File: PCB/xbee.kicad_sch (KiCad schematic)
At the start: 5 parts

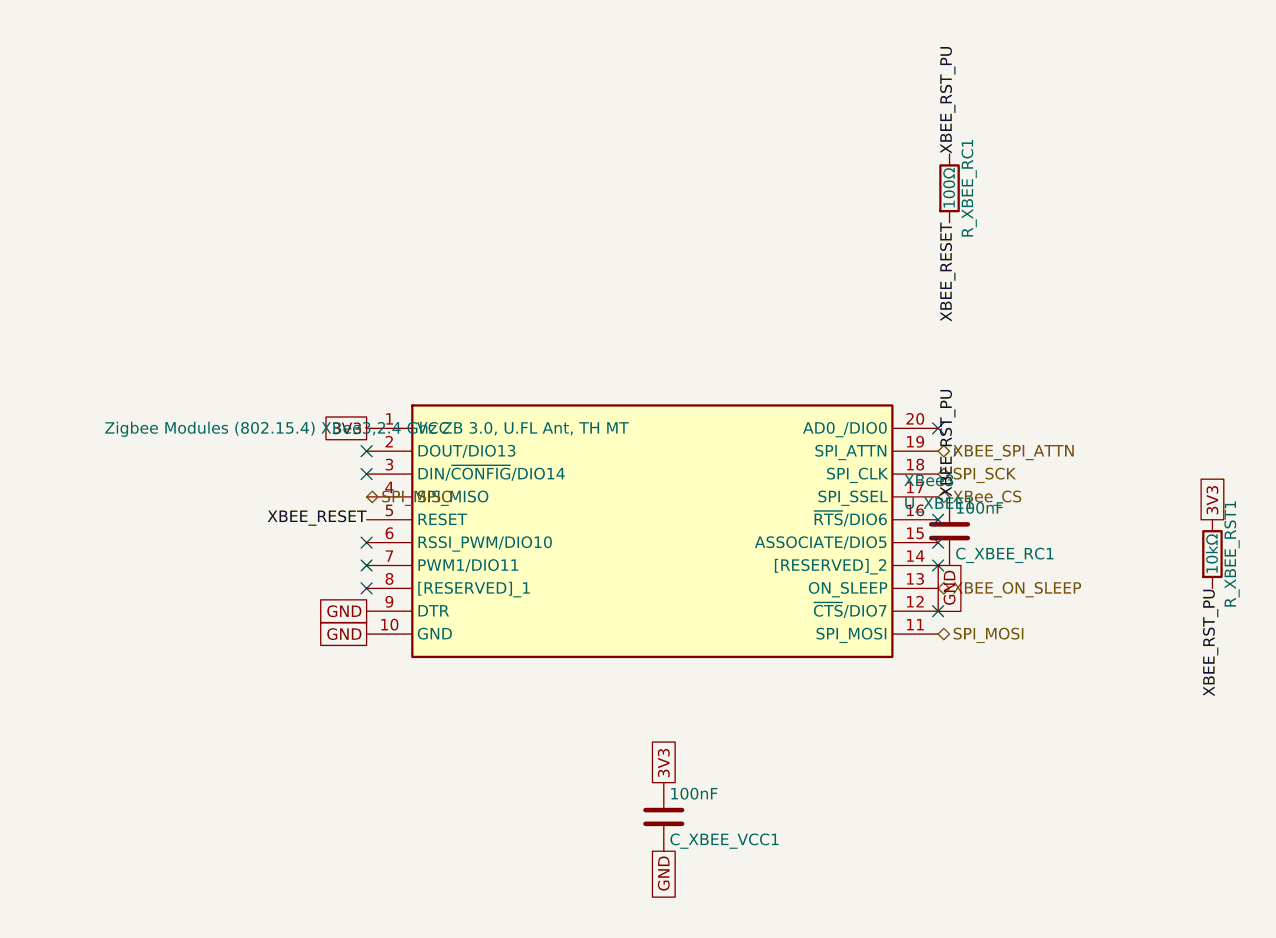
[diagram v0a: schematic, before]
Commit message: refactor: updated gulikit footprint
This updates the gulikit thumbstick footprint to be accurate.
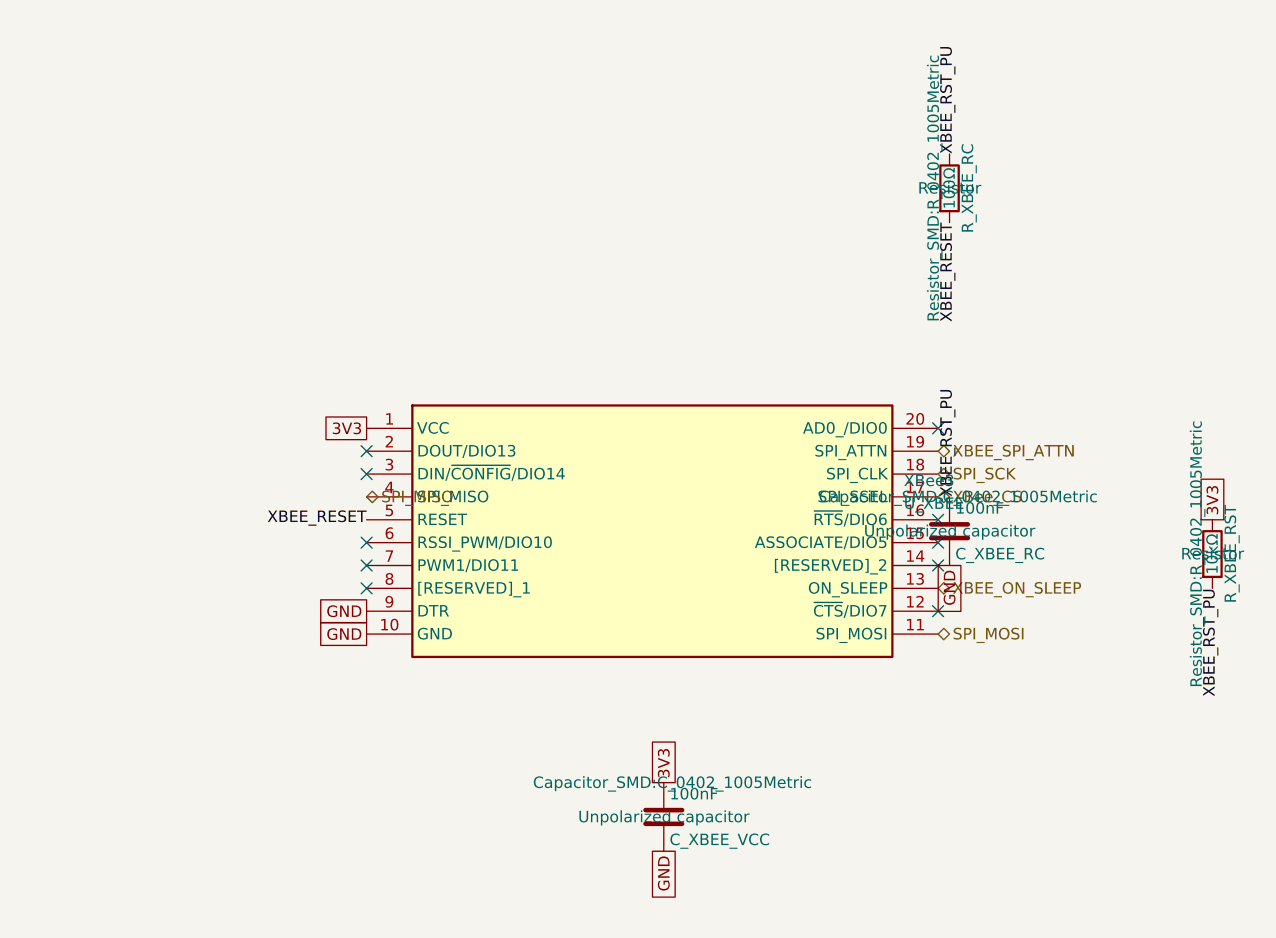
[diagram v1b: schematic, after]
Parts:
- removed C_XBEE_RC1, C_XBEE_VCC1: 100nF, Capacitor_SMD:C_0402_1005Metric, symbol Device:C
- removed R_XBEE_RC1: 100Ω, Resistor_SMD:R_0402_1005Metric, symbol Device:R
- removed R_XBEE_RST1: 10kΩ, Resistor_SMD:R_0402_1005Metric, symbol Device:R
- removed U_XBEE1: XBee3, Xbee3:XB324Z8UTJ, symbol Xbee3:XB3-24Z8UT-J
- added C_XBEE_RC, C_XBEE_VCC: 100nF, Capacitor_SMD:C_0402_1005Metric, symbol Device:C
- added R_XBEE_RC: 100Ω, Resistor_SMD:R_0402_1005Metric, symbol Device:R
- added R_XBEE_RST: 10kΩ, Resistor_SMD:R_0402_1005Metric, symbol Device:R
- added U_XBEE: XBee3, Xbee3:XB324Z8UTJ, symbol Xbee3:XB3-24Z8UT-J
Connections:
- net 3V3: now also C_XBEE_VCC.1, R_XBEE_RST.1, U_XBEE.1 (VCC)
- net GND: now also C_XBEE_RC.2, C_XBEE_VCC.2, U_XBEE.10 (GND), U_XBEE.9 (DTR)
- net SPI_MISO: now also U_XBEE.4 (SPI_MISO)
- net SPI_MOSI: now also U_XBEE.11 (SPI_MOSI)
- net SPI_SCK: now also U_XBEE.18 (SPI_CLK)
- net XBEE_ON_SLEEP: now also U_XBEE.13 (ON_SLEEP)
- net XBEE_RESET: now also R_XBEE_RC.2, U_XBEE.5 (RESET)
- net XBEE_RST_PU: now also C_XBEE_RC.1, R_XBEE_RC.1, R_XBEE_RST.2
- net XBEE_SPI_ATTN: now also U_XBEE.19 (SPI_ATTN)
- net XBee_CS: now also U_XBEE.17 (SPI_SSEL)

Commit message: layout: beginning pcb layout
This updates the schematic with a few different footprints while also starts the layout.
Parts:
- renumbered C_XBEE_RC to C_XBEE_RC1, C_XBEE_VCC to C_XBEE_VCC1, R_XBEE_RC to R_XBEE_RC1, R_XBEE_RST to R_XBEE_RST1, U_XBEE to U_XBEE1
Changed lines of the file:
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@@
 		(dnp no)
 		(fields_autoplaced yes)
-		(property "Reference" "U_XBEE"
+		(property "Reference" "U_XBEE1"
 			(at 161.29 104.14 0)
 			(show_name no)
@@
 			)
 		)
-		(property "Description" ""
+		(property "Description" "Zigbee Modules (802.15.4) XBee3,2.4 Ghz ZB 3.0, U.FL Ant, TH MT"
 			(at 101.6 96.52 0)
 			(show_name no)
@@
 		)
 		(instances
+			(project "snips_controller"
+				(path "/868f8289-8434-4465-b2f4-2accc5e40bab/456186b5-e5fa-459c-a04e-9d51d6afbbb5"
+					(reference "U_XBEE1")
+					(unit 1)
+				)
+			)
 			(project ""
 				(path "/d0f5b7d7-b2b6-4492-958c-e60265d3c6b4/456186b5-e5fa-459c-a04e-9d51d6afbbb5"
@@
 		(dnp no)
 		(fields_autoplaced yes)
-		(property "Reference" "C_XBEE_RC"
+		(property "Reference" "C_XBEE_RC1"
 			(at 167.005 110.49 0)
 			(show_name no)
@@
 		)
 		(instances
+			(project "snips_controller"
+				(path "/868f8289-8434-4465-b2f4-2accc5e40bab/456186b5-e5fa-459c-a04e-9d51d6afbbb5"
+					(reference "C_XBEE_RC1")
+					(unit 1)
+				)
+			)
 			(project ""
 				(path "/d0f5b7d7-b2b6-4492-958c-e60265d3c6b4/456186b5-e5fa-459c-a04e-9d51d6afbbb5"
@@
 		(dnp no)
 		(fields_autoplaced yes)
-		(property "Reference" "C_XBEE_VCC"
+		(property "Reference" "C_XBEE_VCC1"
 			(at 135.255 142.24 0)
 			(show_name no)
@@
 		)
 		(instances
+			(project "snips_controller"
+				(path "/868f8289-8434-4465-b2f4-2accc5e40bab/456186b5-e5fa-459c-a04e-9d51d6afbbb5"
+					(reference "C_XBEE_VCC1")
+					(unit 1)
+				)
+			)
 			(project ""
 				(path "/d0f5b7d7-b2b6-4492-958c-e60265d3c6b4/456186b5-e5fa-459c-a04e-9d51d6afbbb5"
@@
 		(dnp no)
 		(fields_autoplaced yes)
-		(property "Reference" "R_XBEE_RST"
+		(property "Reference" "R_XBEE_RST1"
 			(at 197.612 110.49 90)
 			(show_name no)
@@
 		)
 		(instances
+			(project "snips_controller"
+				(path "/868f8289-8434-4465-b2f4-2accc5e40bab/456186b5-e5fa-459c-a04e-9d51d6afbbb5"
+					(reference "R_XBEE_RST1")
+					(unit 1)
+				)
+			)
 			(project ""
 				(path "/d0f5b7d7-b2b6-4492-958c-e60265d3c6b4/456186b5-e5fa-459c-a04e-9d51d6afbbb5"
@@
 		(dnp no)
 		(fields_autoplaced yes)
-		(property "Reference" "R_XBEE_RC"
+		(property "Reference" "R_XBEE_RC1"
 			(at 168.402 69.85 90)
 			(show_name no)
@@
 		)
 		(instances
+			(project "snips_controller"
+				(path "/868f8289-8434-4465-b2f4-2accc5e40bab/456186b5-e5fa-459c-a04e-9d51d6afbbb5"
+					(reference "R_XBEE_RC1")
+					(unit 1)
+				)
+			)
 			(project ""
 				(path "/d0f5b7d7-b2b6-4492-958c-e60265d3c6b4/456186b5-e5fa-459c-a04e-9d51d6afbbb5"

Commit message: refactor: swap footprints and add symmetry
This updates the footprints of a couple components to be smaller and closer to what we want. It also adds two buttons to ensure left and right side symmetry.
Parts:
- removed C_XBEE_RC1, C_XBEE_VCC1: 100nF, Capacitor_SMD:C_0402_1005Metric, symbol Device:C
- removed R_XBEE_RC1: 100Ω, Resistor_SMD:R_0402_1005Metric, symbol Device:R
- removed R_XBEE_RST1: 10kΩ, Resistor_SMD:R_0402_1005Metric, symbol Device:R
- removed U_XBEE1: XBee3, Xbee3:XB324Z8UTJ, symbol Xbee3:XB3-24Z8UT-J
- added C_XBEE_RC, C_XBEE_VCC: 100nF, Capacitor_SMD:C_0402_1005Metric, symbol Device:C
- added R_XBEE_RC: 100Ω, Resistor_SMD:R_0402_1005Metric, symbol Device:R
- added R_XBEE_RST: 10kΩ, Resistor_SMD:R_0402_1005Metric, symbol Device:R
- added U_XBEE: XBee3, Xbee3:XB324Z8UTJ, symbol Xbee3:XB3-24Z8UT-J
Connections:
- net 3V3: now also C_XBEE_VCC.1, R_XBEE_RST.1, U_XBEE.1 (VCC)
- net GND: now also C_XBEE_RC.2, C_XBEE_VCC.2, U_XBEE.10 (GND), U_XBEE.9 (DTR)
- net SPI_MISO: now also U_XBEE.4 (SPI_MISO)
- net SPI_MOSI: now also U_XBEE.11 (SPI_MOSI)
- net SPI_SCK: now also U_XBEE.18 (SPI_CLK)
- net XBEE_ON_SLEEP: now also U_XBEE.13 (ON_SLEEP)
- net XBEE_RESET: now also R_XBEE_RC.2, U_XBEE.5 (RESET)
- net XBEE_RST_PU: now also C_XBEE_RC.1, R_XBEE_RC.1, R_XBEE_RST.2
- net XBEE_SPI_ATTN: now also U_XBEE.19 (SPI_ATTN)
- net XBee_CS: now also U_XBEE.17 (SPI_SSEL)

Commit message: layout: everything is on the board
The board edge cuts are down to 100mm x 35mm. All the components have the right footprints and are on the board, but no traces exist yet, and not all circuits are laid out properly yet. Lots of DRC warnings.
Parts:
- removed C_XBEE_RC, C_XBEE_VCC: 100nF, Capacitor_SMD:C_0402_1005Metric, symbol Device:C
- removed R_XBEE_RC: 100Ω, Resistor_SMD:R_0402_1005Metric, symbol Device:R
- removed R_XBEE_RST: 10kΩ, Resistor_SMD:R_0402_1005Metric, symbol Device:R
- removed U_XBEE: XBee3, Xbee3:XB324Z8UTJ, symbol Xbee3:XB3-24Z8UT-J
- added C_XBEE_RC1, C_XBEE_VCC1: 100nF, Capacitor_SMD:C_0402_1005Metric, symbol Device:C
- added R_XBEE_RC1: 100Ω, Resistor_SMD:R_0402_1005Metric, symbol Device:R
- added R_XBEE_RST1: 10kΩ, Resistor_SMD:R_0402_1005Metric, symbol Device:R
- added U_XBEE1: XBee3, Xbee3:XB324Z8UTJ, symbol Xbee3:XB3-24Z8UT-J
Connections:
- net 3V3: now also C_XBEE_VCC1.1, R_XBEE_RST1.1, U_XBEE1.1 (VCC)
- net GND: now also C_XBEE_RC1.2, C_XBEE_VCC1.2, U_XBEE1.10 (GND), U_XBEE1.9 (DTR)
- net SPI_MISO: now also U_XBEE1.4 (SPI_MISO)
- net SPI_MOSI: now also U_XBEE1.11 (SPI_MOSI)
- net SPI_SCK: now also U_XBEE1.18 (SPI_CLK)
- net XBEE_ON_SLEEP: now also U_XBEE1.13 (ON_SLEEP)
- net XBEE_RESET: now also R_XBEE_RC1.2, U_XBEE1.5 (RESET)
- net XBEE_RST_PU: now also C_XBEE_RC1.1, R_XBEE_RC1.1, R_XBEE_RST1.2
- net XBEE_SPI_ATTN: now also U_XBEE1.19 (SPI_ATTN)
- net XBee_CS: now also U_XBEE1.17 (SPI_SSEL)

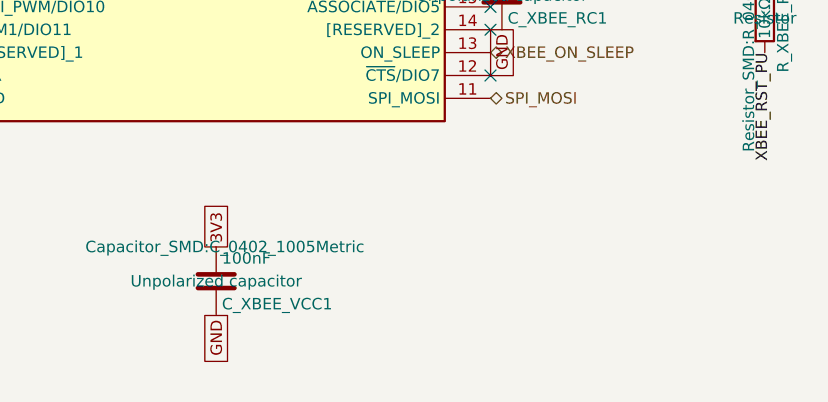
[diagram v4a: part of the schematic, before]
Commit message: refactor: tracing and diagrams
Adding traces and laying out circuits for the buck, planning for the power and charging circuits.
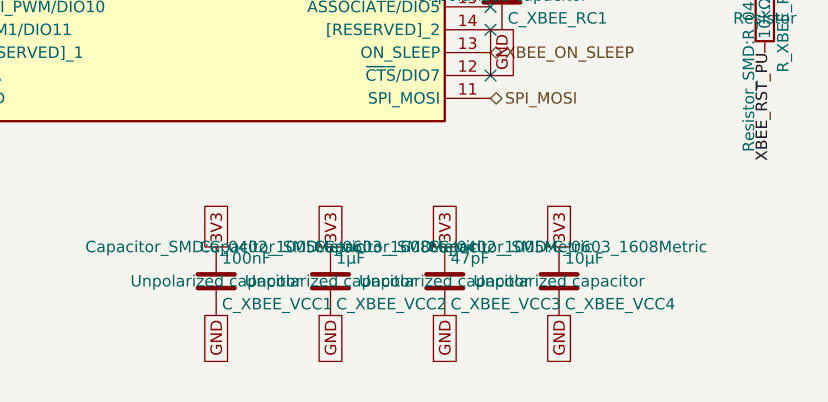
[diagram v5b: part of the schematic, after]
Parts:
- added C_XBEE_VCC2: 1µF, Capacitor_SMD:C_0603_1608Metric, symbol Device:C
- added C_XBEE_VCC3: 47pF, Capacitor_SMD:C_0402_1005Metric, symbol Device:C
- added C_XBEE_VCC4: 10µF, Capacitor_SMD:C_0603_1608Metric, symbol Device:C
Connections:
- net 3V3: now also C_XBEE_VCC2.1, C_XBEE_VCC3.1, C_XBEE_VCC4.1
- net GND: now also C_XBEE_VCC2.2, C_XBEE_VCC3.2, C_XBEE_VCC4.2

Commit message: task: part number populated (#26)
kicad-happy run part 2 - MPN numbers populated
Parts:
- C_XBEE_RC1, C_XBEE_VCC1: MF (none) -> Yageo; Manufacturer_Part_Number (none) -> CC0402KRX7R9BB104
- C_XBEE_VCC2: MF (none) -> Yageo; Manufacturer_Part_Number (none) -> CC0603KRX5R7BB105
- C_XBEE_VCC3: MF (none) -> Yageo; Manufacturer_Part_Number (none) -> CC0402JRNPO9BN470
- C_XBEE_VCC4: MF (none) -> Yageo; Manufacturer_Part_Number (none) -> CC0603KRX5R7BB106
- R_XBEE_RC1: MF (none) -> Yageo; Manufacturer_Part_Number (none) -> RC0402FR-07100RL
- R_XBEE_RST1: MF (none) -> Yageo; Manufacturer_Part_Number (none) -> RC0402FR-0710KL
- U_XBEE1: MF (none) -> Digi International
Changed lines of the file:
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@@
+			)
+		)
+		(property "MF" "Yageo" (at 0 0 0)
+			(effects
+				(font
+					(size 1.27 1.27)
+				)
+				(hide yes)
+			)
+		)
+		(property "Manufacturer_Part_Number" "CC0402JRNPO9BN470" (at 0 0 0)
+			(effects
+				(font
+					(size 1.27 1.27)
+				)
+				(hide yes)
 			)
 		)
@@
 			)
 		)
+		(property "MF" "Digi International" (at 0 0 0)
+			(effects
+				(font
+					(size 1.27 1.27)
+				)
+				(hide yes)
+			)
+		)
 		(pin "1"
 		)
@@
 			)
 		)
+		(property "MF" "Yageo" (at 0 0 0)
+			(effects
+				(font
+					(size 1.27 1.27)
+				)
+				(hide yes)
+			)
+		)
+		(property "Manufacturer_Part_Number" "CC0603KRX5R7BB105" (at 0 0 0)
+			(effects
+				(font
+					(size 1.27 1.27)
+				)
+				(hide yes)
+			)
+		)
 		(pin "1"
 		)
@@
 			)
 		)
+		(property "MF" "Yageo" (at 0 0 0)
+			(effects
+				(font
+					(size 1.27 1.27)
+				)
+				(hide yes)
+			)
+		)
+		(property "Manufacturer_Part_Number" "CC0603KRX5R7BB106" (at 0 0 0)
+			(effects
+				(font
+					(size 1.27 1.27)
+				)
+				(hide yes)
+			)
+		)
 		(pin "1"
 		)
@@
 			)
 		)
+		(property "MF" "Yageo" (at 0 0 0)
+			(effects
+				(font
+					(size 1.27 1.27)
+				)
+				(hide yes)
+			)
+		)
+		(property "Manufacturer_Part_Number" "CC0402KRX7R9BB104" (at 0 0 0)
+			(effects
+				(font
+					(size 1.27 1.27)
+				)
+				(hide yes)
+			)
+		)
 		(pin "1"
 		)
@@
 			)
 		)
+		(property "MF" "Yageo" (at 0 0 0)
+			(effects
+				(font
+					(size 1.27 1.27)
+				)
+				(hide yes)
+			)
+		)
+		(property "Manufacturer_Part_Number" "RC0402FR-0710KL" (at 0 0 0)
+			(effects
+				(font
+					(size 1.27 1.27)
+				)
+				(hide yes)
+			)
+		)
 		(pin "1"
 		)
@@
 			)
 		)
+		(property "MF" "Yageo" (at 0 0 0)
+			(effects
+				(font
+					(size 1.27 1.27)
+				)
+				(hide yes)
+			)
+		)
+		(property "Manufacturer_Part_Number" "RC0402FR-07100RL" (at 0 0 0)
+			(effects
+				(font
+					(size 1.27 1.27)
+				)
+				(hide yes)
+			)
+		)
 		(pin "1"
 		)
@@
 			)
 		)
+		(property "MF" "Yageo" (at 0 0 0)
+			(effects
+				(font
+					(size 1.27 1.27)
+				)
+				(hide yes)
+			)
+		)
+		(property "Manufacturer_Part_Number" "CC0402KRX7R9BB104" (at 0 0 0)
+			(effects
+				(font
+					(size 1.27 1.27)
+				)
+				(hide yes)
+			)
+		)

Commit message: task: generate production files (#27)
* task: generate production files

We have wrapped up board validation. Gerbers are now generated. Logo generated. Good to go.

* refactor: added STAT2

It was worth adding and will give us more info during battery charging.
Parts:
- U_XBEE1: now left out of the parts list
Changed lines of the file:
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@@
 			)
 		)
-		(property "MF" "Yageo" (at 0 0 0)
-			(effects
-				(font
-					(size 1.27 1.27)
-				)
-				(hide yes)
-			)
-		)
-		(property "Manufacturer_Part_Number" "CC0402JRNPO9BN470" (at 0 0 0)
-			(effects
-				(font
-					(size 1.27 1.27)
-				)
-				(hide yes)
+		(property "MF" "Yageo"
+			(at 0 0 0)
+			(hide yes)
+			(show_name no)
+			(do_not_autoplace no)
+			(effects
+				(font
+					(size 1.27 1.27)
+				)
+			)
+		)
+		(property "Manufacturer_Part_Number" "CC0402JRNPO9BN470"
+			(at 0 0 0)
+			(hide yes)
+			(show_name no)
+			(do_not_autoplace no)
+			(effects
+				(font
+					(size 1.27 1.27)
+				)
 			)
 		)
@@
 		(body_style 1)
 		(exclude_from_sim no)
-		(in_bom yes)
+		(in_bom no)
 		(on_board yes)
 		(in_pos_files yes)
@@
 			)
 		)
-		(property "MF" "Digi International" (at 0 0 0)
-			(effects
-				(font
-					(size 1.27 1.27)
-				)
-				(hide yes)
+		(property "MF" "Digi International"
+			(at 0 0 0)
+			(hide yes)
+			(show_name no)
+			(do_not_autoplace no)
+			(effects
+				(font
+					(size 1.27 1.27)
+				)
 			)
 		)
@@
 			)
 		)
-		(property "MF" "Yageo" (at 0 0 0)
-			(effects
-				(font
-					(size 1.27 1.27)
-				)
-				(hide yes)
-			)
-		)
-		(property "Manufacturer_Part_Number" "CC0603KRX5R7BB105" (at 0 0 0)
-			(effects
-				(font
-					(size 1.27 1.27)
-				)
-				(hide yes)
+		(property "MF" "Yageo"
+			(at 0 0 0)
+			(hide yes)
+			(show_name no)
+			(do_not_autoplace no)
+			(effects
+				(font
+					(size 1.27 1.27)
+				)
+			)
+		)
+		(property "Manufacturer_Part_Number" "CC0603KRX5R7BB105"
+			(at 0 0 0)
+			(hide yes)
+			(show_name no)
+			(do_not_autoplace no)
+			(effects
+				(font
+					(size 1.27 1.27)
+				)
 			)
 		)
@@
 			)
 		)
-		(property "MF" "Yageo" (at 0 0 0)
-			(effects
-				(font
-					(size 1.27 1.27)
-				)
-				(hide yes)
-			)
-		)
-		(property "Manufacturer_Part_Number" "CC0603KRX5R7BB106" (at 0 0 0)
-			(effects
-				(font
-					(size 1.27 1.27)
-				)
-				(hide yes)
+		(property "MF" "Yageo"
+			(at 0 0 0)
+			(hide yes)
+			(show_name no)
+			(do_not_autoplace no)
+			(effects
+				(font
+					(size 1.27 1.27)
+				)
+			)
+		)
+		(property "Manufacturer_Part_Number" "CC0603KRX5R7BB106"
+			(at 0 0 0)
+			(hide yes)
+			(show_name no)
+			(do_not_autoplace no)
+			(effects
+				(font
+					(size 1.27 1.27)
+				)
 			)
 		)
@@
 			)
 		)
-		(property "MF" "Yageo" (at 0 0 0)
-			(effects
-				(font
-					(size 1.27 1.27)
-				)
-				(hide yes)
-			)
-		)
-		(property "Manufacturer_Part_Number" "CC0402KRX7R9BB104" (at 0 0 0)
-			(effects
-				(font
-					(size 1.27 1.27)
-				)
-				(hide yes)
+		(property "MF" "Yageo"
+			(at 0 0 0)
+			(hide yes)
+			(show_name no)
+			(do_not_autoplace no)
+			(effects
+				(font
+					(size 1.27 1.27)
+				)
+			)
+		)
+		(property "Manufacturer_Part_Number" "CC0402KRX7R9BB104"
+			(at 0 0 0)
+			(hide yes)
+			(show_name no)
+			(do_not_autoplace no)
+			(effects
+				(font
+					(size 1.27 1.27)
+				)
 			)
 		)
@@
 			)
 		)
-		(property "MF" "Yageo" (at 0 0 0)
-			(effects
-				(font
-					(size 1.27 1.27)
-				)
-				(hide yes)
-			)
-		)
-		(property "Manufacturer_Part_Number" "RC0402FR-0710KL" (at 0 0 0)
-			(effects
-				(font
-					(size 1.27 1.27)
-				)
-				(hide yes)
+		(property "MF" "Yageo"
+			(at 0 0 0)
+			(hide yes)
+			(show_name no)
+			(do_not_autoplace no)
+			(effects
+				(font
+					(size 1.27 1.27)
+				)
+			)
+		)
+		(property "Manufacturer_Part_Number" "RC0402FR-0710KL"
+			(at 0 0 0)
+			(hide yes)
+			(show_name no)
+			(do_not_autoplace no)
+			(effects
+				(font
+					(size 1.27 1.27)
+				)
 			)
 		)
@@
 			)
 		)
-		(property "MF" "Yageo" (at 0 0 0)
-			(effects
-				(font
-					(size 1.27 1.27)
-				)
-				(hide yes)
-			)
-		)
-		(property "Manufacturer_Part_Number" "RC0402FR-07100RL" (at 0 0 0)
-			(effects
-				(font
-					(size 1.27 1.27)
-				)
-				(hide yes)
+		(property "MF" "Yageo"
+			(at 0 0 0)
+			(hide yes)
+			(show_name no)
+			(do_not_autoplace no)
+			(effects
+				(font
+					(size 1.27 1.27)
+				)
+			)
+		)
+		(property "Manufacturer_Part_Number" "RC0402FR-07100RL"
+			(at 0 0 0)
+			(hide yes)
+			(show_name no)
+			(do_not_autoplace no)
+			(effects
+				(font
+					(size 1.27 1.27)
+				)
 			)
 		)
@@
 			)
 		)
-		(property "MF" "Yageo" (at 0 0 0)
-			(effects
-				(font
-					(size 1.27 1.27)
-				)
-				(hide yes)
-			)
-		)
-		(property "Manufacturer_Part_Number" "CC0402KRX7R9BB104" (at 0 0 0)
-			(effects
-				(font
-					(size 1.27 1.27)
-				)
-				(hide yes)
-			)
-		)
+		(property "MF" "Yageo"
+			(at 0 0 0)
+			(hide yes)
+			(show_name no)
+			(do_not_autoplace no)
+			(effects
+				(font
+					(size 1.27 1.27)
+				)
+			)
+		)
+		(property "Manufacturer_Part_Number" "CC0402KRX7R9BB104"
+			(at 0 0 0)
+			(hide yes)
+			(show_name no)
+			(do_not_autoplace no)
+			(effects
+				(font
+					(size 1.27 1.27)
+				)
+			)
+		)
